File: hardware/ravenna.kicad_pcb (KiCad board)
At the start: 4 copper layers, 22.9 x 54.6 mm, 63 parts, among them IC1 RAVENAQFN56, IC2 FT232H, IC3 MCP1755, IC4 93C56, J1 629105150521, J2 Conn_01x02_Male, J3 2X6 FEMALE, J4 CONN_20, J5 CONN_20, U1 SN74LVC1G125DCKR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

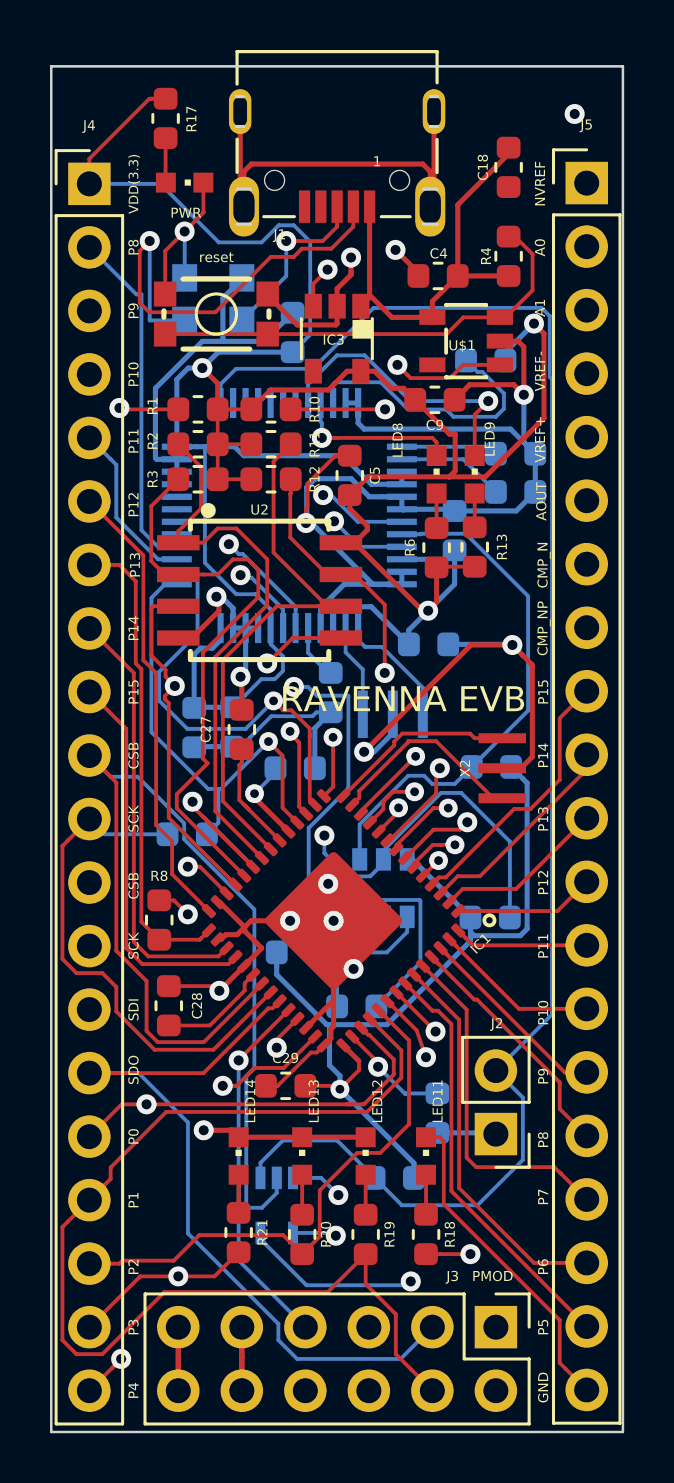
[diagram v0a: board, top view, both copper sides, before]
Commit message: add gerbers; updated silkscreen
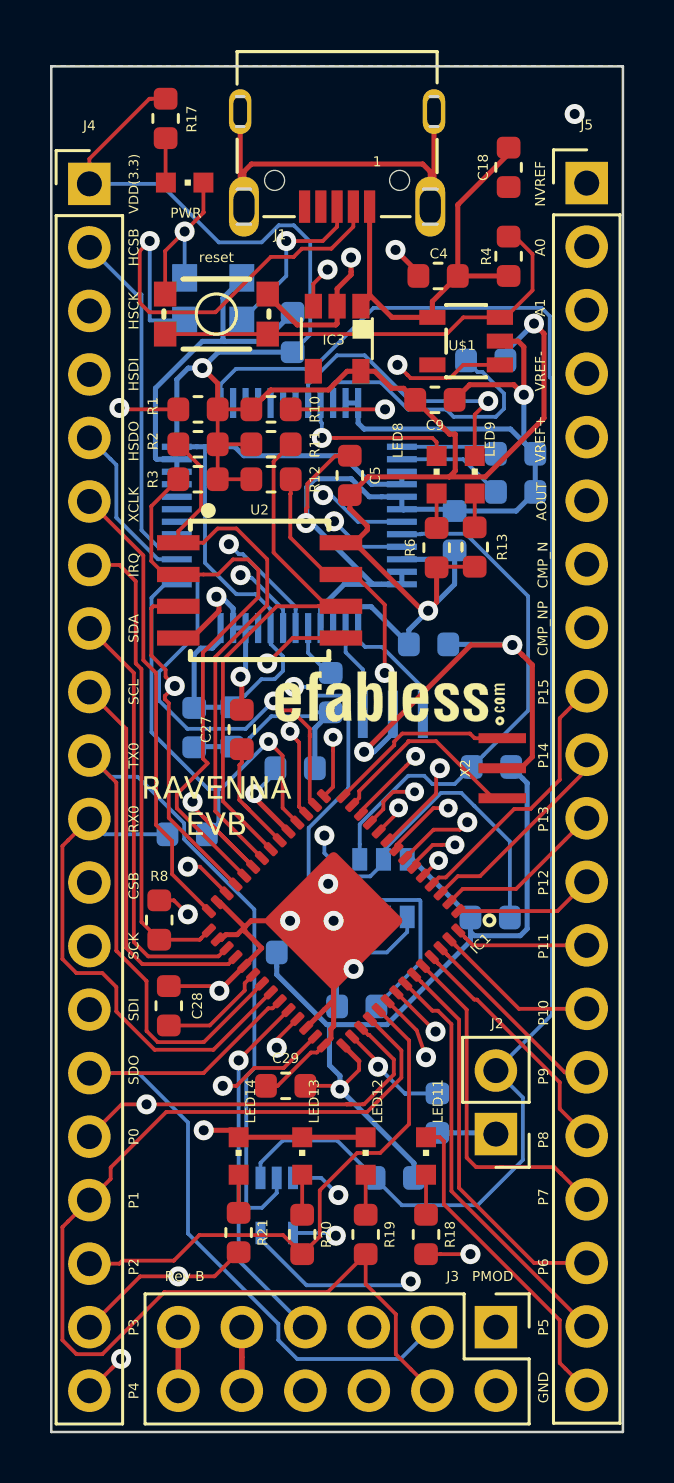
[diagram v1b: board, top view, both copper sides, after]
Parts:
- added G***: LOGO, parts and footprints:logo, F.Cu at (150.5, 106.3)
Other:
- board text added: "HCSB"
- board text added: "HSCK"
- board text added: "HSDI"
- board text added: "HSDO"
- board text added: "IRQ"
- board text added: "RX0"
- board text added: "Rev B"
- board text added: "SCL"
- board text added: "SDA"
- board text added: "TX0"
- board text added: "XCLK"

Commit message: fixed gnd pad for switch; fixed courtyard overlaps;
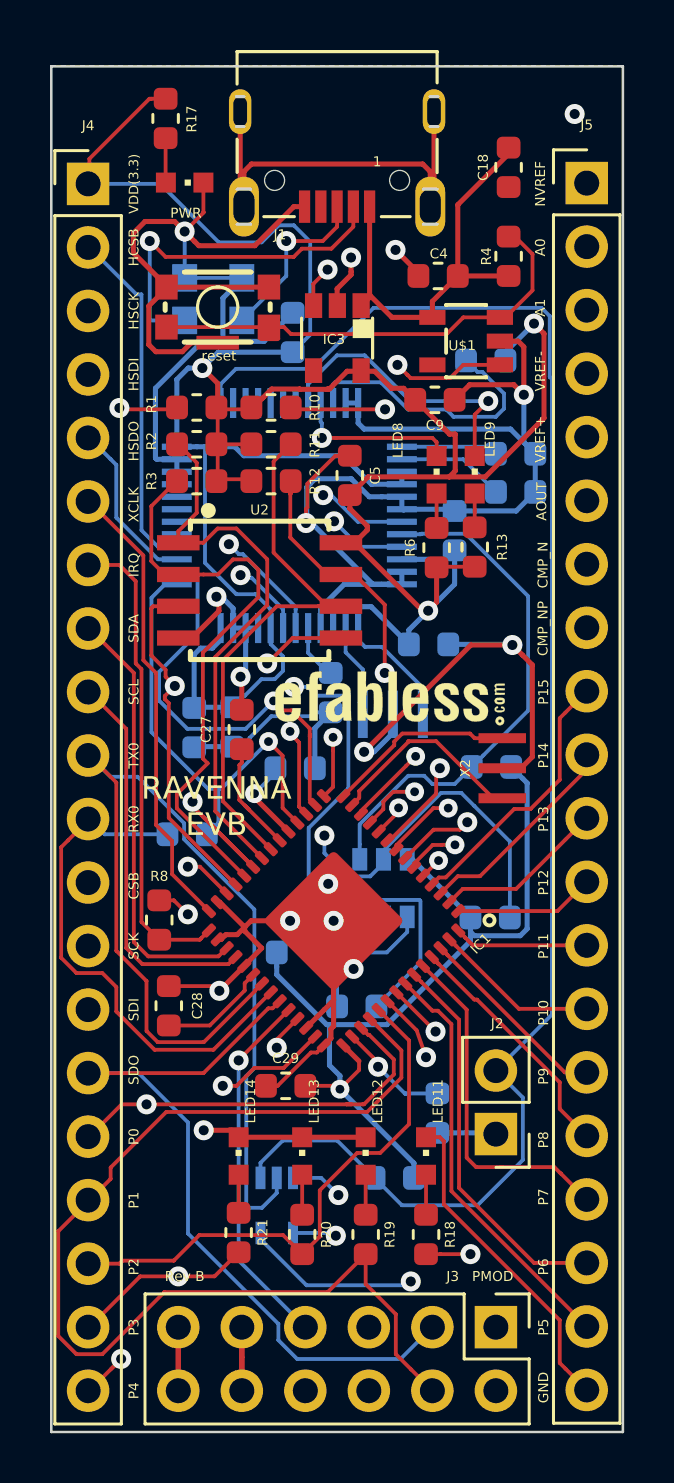
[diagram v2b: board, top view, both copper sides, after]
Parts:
- moved RESET1 0.28 mm to (143.7, 90.7)
- moved R1 0.09 mm to (142.8, 94.7)
- moved R3 0.09 mm to (142.8, 97.6)
- moved R10 0.08 mm to (145.8, 94.7)
- moved R12 0.08 mm to (145.8, 97.6)
- moved J4 0.05 mm to (138.5, 85.7)
- moved R2 0.05 mm to (142.8, 96.1)
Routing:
- net GND: track 241.9 -> 255.7 mm
- net Net-(FUSE1-Pad2): track 36.4 -> 32.5 mm
- net Net-(R4-Pad1): track 17.9 -> 18.6 mm
